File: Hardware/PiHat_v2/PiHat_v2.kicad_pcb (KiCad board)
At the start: 2 copper layers, 64 x 55 mm, 23 parts

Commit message: Make the PCB Pretty Again (#134)
* Implement OSHW Copper Logo on PiHAT

* Implement CI, Makerspace, Paw Logo on PiHAT

* Archive final PiHAT_v0.2.1 Design

This is a simple .zip archive of the final PiHAT_v0.2.1 design.

* Redraw Fill Zones on PiHAT v0.2.1

Whoops - Forgot to redraw the fill zones. That's been remedied!
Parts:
- added G***: LOGO, .pretty:makerspace_4,8mm, F.Cu at (146.3, 107.2)
- added G***: LOGO, .pretty:ci_wide_6mm, B.Cu at (145.4, 106.4)
- added G***: LOGO, .pretty:tiger_paw_10mm, F.Cu at (126.0, 89.5)
- added G***: LOGO, .pretty:tiger_paw_10mm, B.Cu at (126.0, 89.5)
- added OSHW_COPPER_10MM: VAL**, oshw-logo-kicad-copper-10mm:OSHW_COPPER_10MM, F.Cu at (110.4, 94.5)

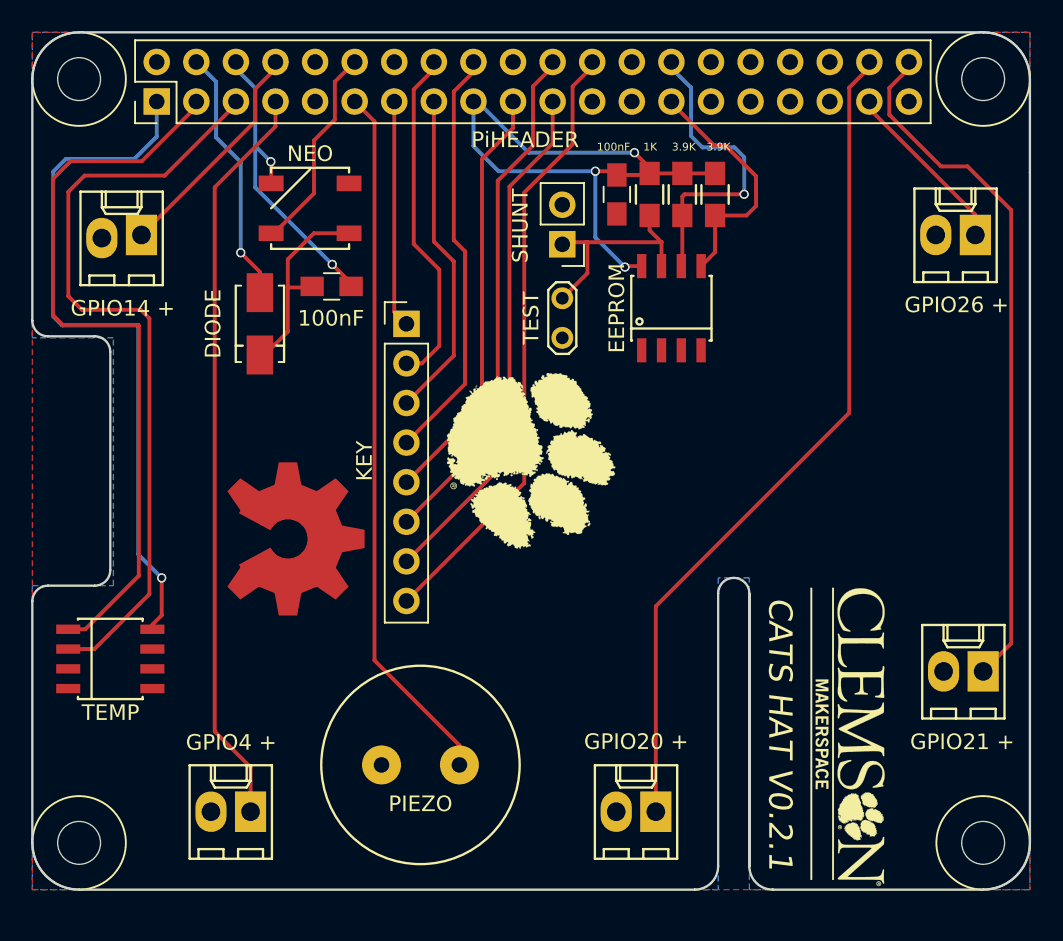
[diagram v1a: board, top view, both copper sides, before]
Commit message: New PCB With ATMEGA Chip (#148)
* Update README.md

Added a period to the end of the sentence

* New Schematic for PiHat

* Finished PiHat v2 Design

* Neopixel Footprint Fix

Rearranged the neopixel terminals to correctly mount it. Moved around
silk screen references and changed the text to better understand the
design when soldering. Added the developers' names to the back of the
board.

* PiHat Completion

References for footprints are placed and named more efficiently. The pi
header footprint is now on the back of the board and all connections to
it were corrected. Added "+"s to the AUX references to show which side
is positive and those reference texts are now what GPIO pin connects to
it. Some footprints that are for components that are polarized or need
to be placed a certain way were redone to show the orientation of the
component for more efficient placement.

* Revert "PiHat Completion"

This reverts commit 6738365f23747a299ba35bc740daefcfdec640b0.

* Revert "Revert "PiHat Completion""

This reverts commit 9dfad16c77172f9cc3f0b0126633a712500f49b7.

* New PCB With ATMEGA

This includes installing the ATMEGA chip for controlling the neopixel
and piezo buzzer. A new piezo for louder sound was added as well.
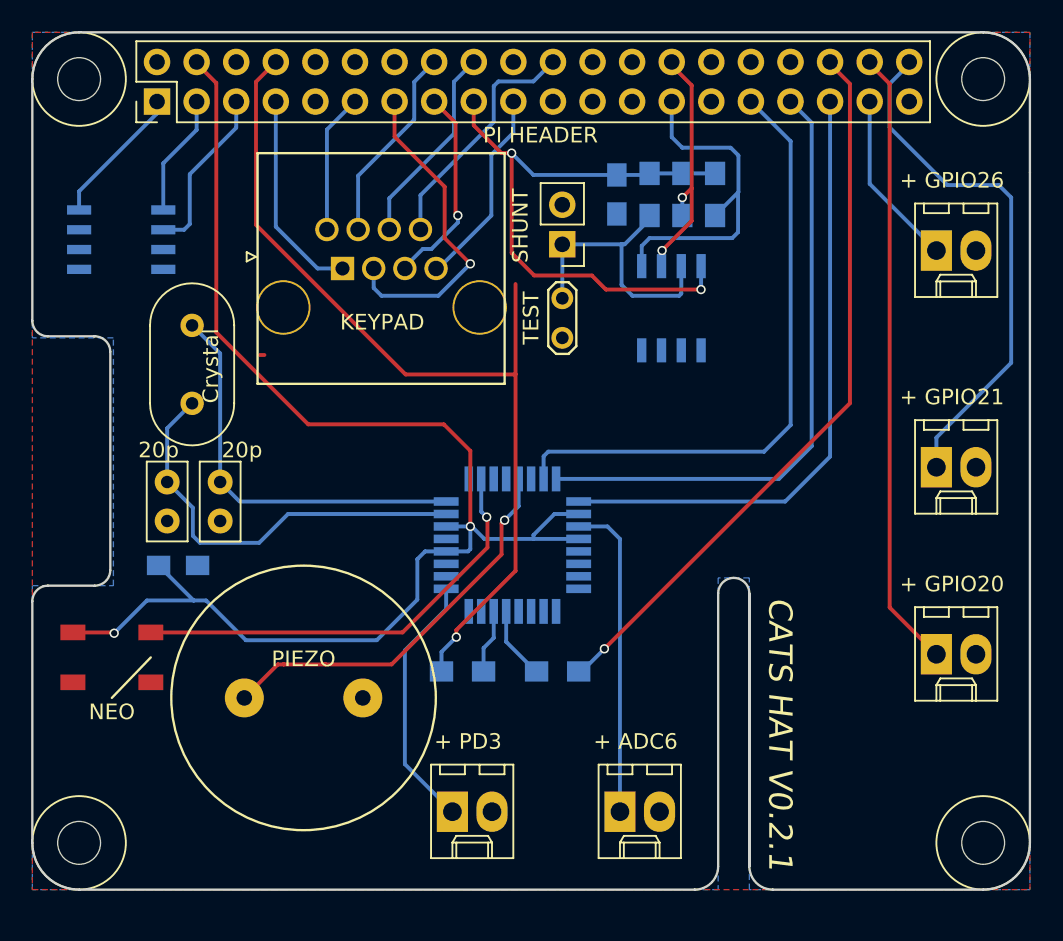
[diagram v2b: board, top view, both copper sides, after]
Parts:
- removed the 100nF at (113.2, 78.3)
- removed DIODE: D_Schottky, .pretty:Schottky_Diode
- removed G***: LOGO, .pretty:makerspace_4,8mm
- removed G***: LOGO, .pretty:ci_wide_6mm
- removed G*** (x2): LOGO, .pretty:tiger_paw_10mm
- removed GPIO14 +: CONN_01X02, Connectors_Molex:Molex_KK-6410-02_02x2.54mm_Straight
- removed GPIO20 +: CONN_01X02, Connectors_Molex:Molex_KK-6410-02_02x2.54mm_Straight
- removed GPIO21 +: CONN_01X02, Connectors_Molex:Molex_KK-6410-02_02x2.54mm_Straight
- removed GPIO26 +: CONN_01X02, Connectors_Molex:Molex_KK-6410-02_02x2.54mm_Straight
- removed GPIO4 +: CONN_01X02, Connectors_Molex:Molex_KK-6410-02_02x2.54mm_Straight
- removed KEY: CONN_01X08, Pin_Headers:Pin_Header_Straight_1x08_Pitch2.54mm
- removed the NEO at (111.8, 73.3)
- removed OSHW_COPPER_10MM: VAL**, oshw-logo-kicad-copper-10mm:OSHW_COPPER_10MM
- removed the PIEZO at (118.9, 109.0)
- removed PiHEADER: CONN_02X20, Pin_Headers:Pin_Header_Straight_2x20_Pitch2.54mm
- added + ADC6: CONN_01X02, Connectors_Molex:Molex_KK-6410-02_02x2.54mm_Straight, F.Cu at (131.7, 112.0)
- added + GPIO20: CONN_01X02, Connectors_Molex:Molex_KK-6410-02_02x2.54mm_Straight, F.Cu at (152.0, 101.9)
- added + GPIO21: CONN_01X02, Connectors_Molex:Molex_KK-6410-02_02x2.54mm_Straight, F.Cu at (152.0, 89.9)
- added + GPIO26: CONN_01X02, Connectors_Molex:Molex_KK-6410-02_02x2.54mm_Straight, F.Cu at (152.0, 76.0)
- added + PD3: CONN_01X02, Connectors_Molex:Molex_KK-6410-02_02x2.54mm_Straight, F.Cu at (121.0, 112.0)
- added 100n: 100n, Capacitors_SMD:C_0805_HandSoldering, B.Cu at (103.3, 96.2)
- added 10k: 10K, Resistors_SMD:R_0805_HandSoldering, B.Cu at (127.7, 103.0)
- added 1k: 1K, Resistors_SMD:R_0805_HandSoldering, B.Cu at (121.6, 103.0)
- added 20p: 20p, Capacitors_THT:C_Disc_D5.0mm_W2.5mm_P2.50mm, F.Cu at (102.7, 93.3)
- added 20p: 20p, Capacitors_THT:C_Disc_D5.0mm_W2.5mm_P2.50mm, F.Cu at (106.0, 93.3)
- added ATMEGA1: ATMEGA328P-A, .pretty:ATMEGA328P, B.Cu at (124.8, 94.9)
- added Crystal: 16 MHz Crystal, Crystals:Resonator-2pin_w10.0mm_h5.0mm, F.Cu at (104.2, 85.8)
- added KEYPAD: CONN_01X08, .pretty:Keypad_Ethernet, F.Cu at (113.9, 77.2)
- added NEO: Neo_LED_RGB_IC, Neo_RGB_LED, F.Cu at (99.1, 102.1)
- added PI HEADER: CONN_02X20, Pin_Headers:Pin_Header_Straight_2x20_Pitch2.54mm, F.Cu at (102.0, 66.4)
- added PIEZO: Piezo, PIEZO, F.Cu at (111.4, 104.7)
- 100nF, 1K, 3.9K (x2), EEPROM, TEMP: moved to B.Cu
- moved TEMP 26.9 mm to (99.7, 75.3), turned to 180 degrees
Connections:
- TEMP pad 5: Net-(temp1-Pad5) -> GND
- TEMP pad 6: Net-(temp1-Pad6) -> GND
- TEMP pad 7: Net-(temp1-Pad7) -> GND
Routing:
- net +5V: track 19.2 -> 91.7 mm, vias 1 -> 2
- net /UART_TXD: track 0.00 -> 59.6 mm, vias 0 -> 1
- net /GPIO16: track 0.08 -> 47.0 mm, vias 0 -> 1
- net /GPIO19: track 0.22 -> 40.3 mm
- net /GPIO6: track 0.00 -> 39.9 mm
- net /GPIO13: track 0.00 -> 39.9 mm
- net /GPIO8: track 39.7 -> 0.51 mm
- net /GPIO2: track 49.9 -> 10.7 mm
- net /GPIO3: track 50.4 -> 11.5 mm
- net +3V3: track 86.8 -> 48.9 mm, vias 4 -> 2
- net /GPIO17: track 45.4 -> 9.12 mm
- net /GPIO4: track 48.1 -> 13.4 mm
- net /GPIO9: track 33.4 -> 0.03 mm
- net /PD6: track 0.00 -> 28.4 mm, vias 0 -> 1
- net Net-(ATMEGA1-Pad7): track 0.00 -> 27.0 mm
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
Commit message: Fixes #148 (#149)
* Update README.md

Added a period to the end of the sentence

* New Schematic for PiHat

* Finished PiHat v2 Design

* Neopixel Footprint Fix

Rearranged the neopixel terminals to correctly mount it. Moved around
silk screen references and changed the text to better understand the
design when soldering. Added the developers' names to the back of the
board.

* PiHat Completion

References for footprints are placed and named more efficiently. The pi
header footprint is now on the back of the board and all connections to
it were corrected. Added "+"s to the AUX references to show which side
is positive and those reference texts are now what GPIO pin connects to
it. Some footprints that are for components that are polarized or need
to be placed a certain way were redone to show the orientation of the
component for more efficient placement.

* Revert "PiHat Completion"

This reverts commit 6738365f23747a299ba35bc740daefcfdec640b0.

* Revert "Revert "PiHat Completion""

This reverts commit 9dfad16c77172f9cc3f0b0126633a712500f49b7.

* New PCB With ATMEGA

This includes installing the ATMEGA chip for controlling the neopixel
and piezo buzzer. A new piezo for louder sound was added as well.

* Remove Invalid Lines in KiCad .pro file

These lines don't belong - they have nothing to do with KiCad.
@thorbrockman did you do something weird when merging commits?

* Remove Unnecessary Git Merge Lines

smh @thorbrockman

* Correct Extra Blank Lines in Schematic

* Implement Blank Line Reduction in Other Packages

* Increment Version Number on PCB

* Update KiCad Project Timestamp
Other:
- board text added: "CATS HAT V0.2.2"
- board text removed: "CATS HAT V0.2.1"
